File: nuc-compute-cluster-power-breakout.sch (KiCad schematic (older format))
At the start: 15 parts, among them J2 BM04B-SRSS-TB-LF-SN, J3 BM04B-SRSS-TB-LF-SN, J5 430450812, J6 430450812, J7 430450812, J8 430450812, J9 430450812, Q11 BC856,215

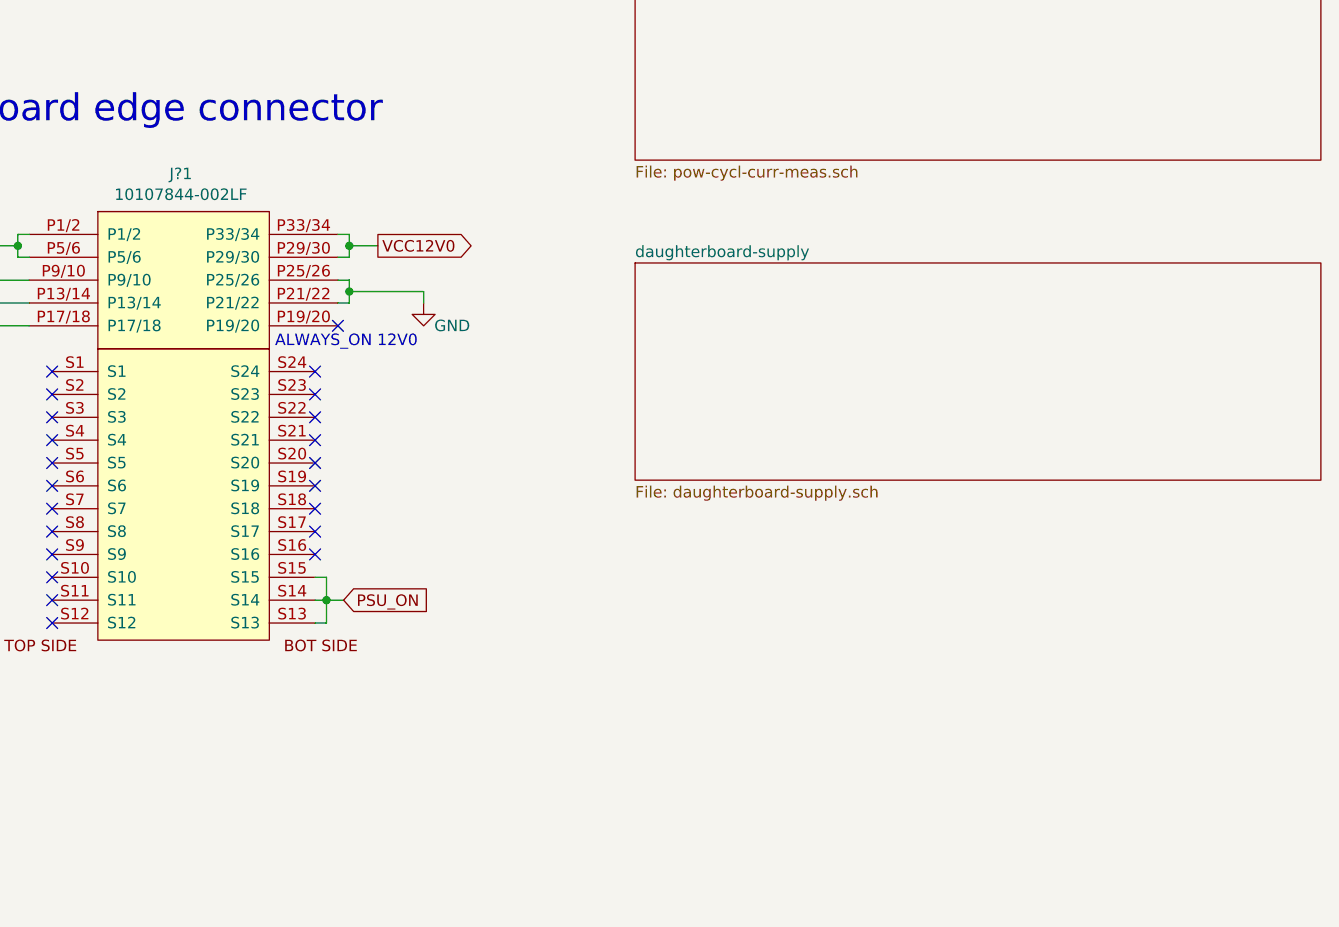
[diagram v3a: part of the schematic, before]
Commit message: Added stitching and mounting holes
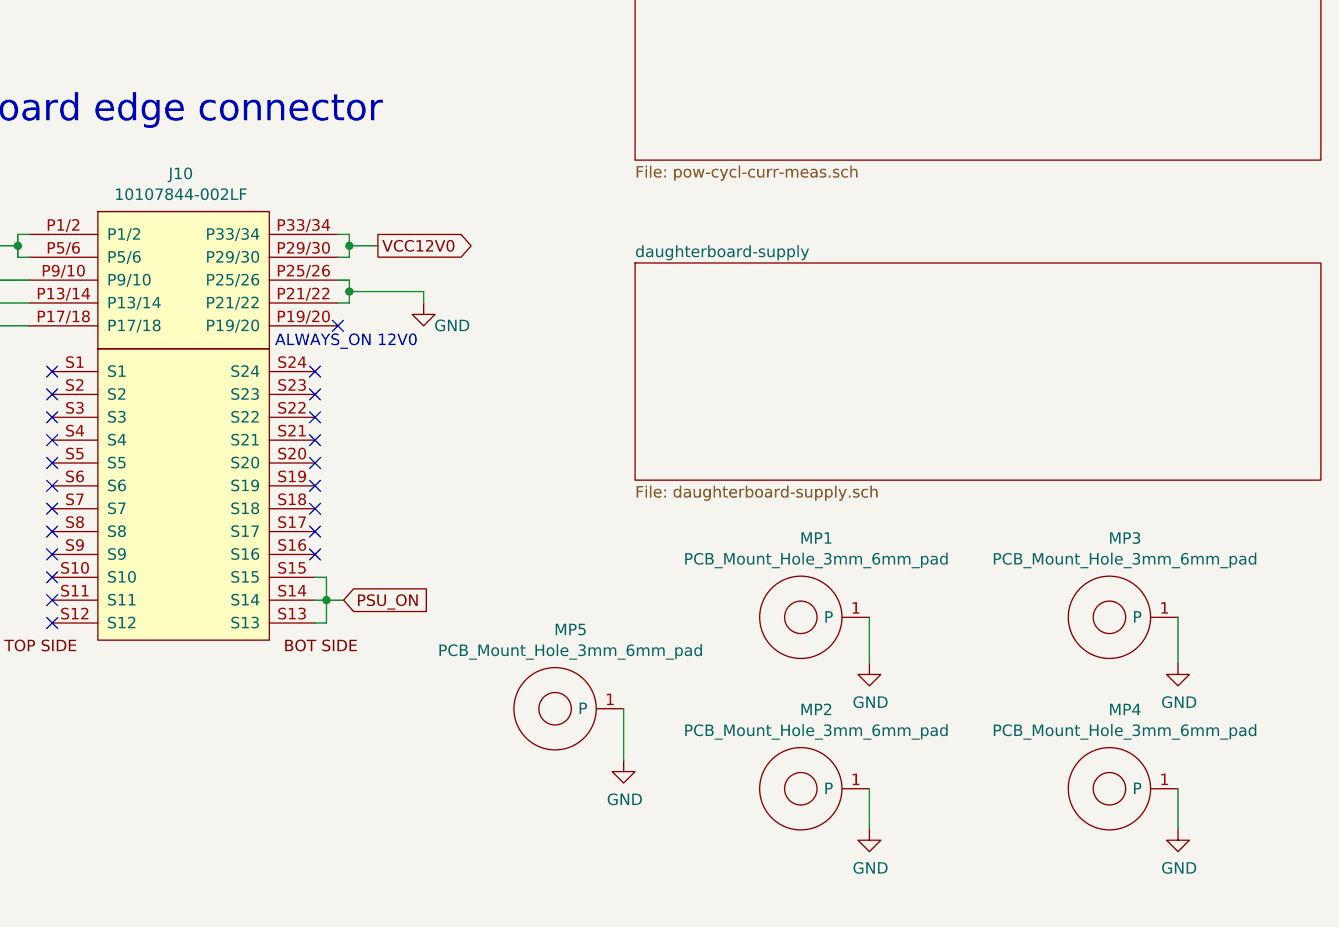
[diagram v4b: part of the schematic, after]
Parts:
- added MP1, MP2, MP3, MP4, MP5: PCB_Mount_Hole_3mm_6mm_pad, antmicro-footprints:mounting-hole-3.2mm, symbol antmicroMechanicalParts:PCB_Mount_Hole_3mm_6mm_pad
- renumbered J?1 to J10
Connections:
- net GND: now also MP1.1 (P), MP2.1 (P), MP3.1 (P), MP4.1 (P), MP5.1 (P)
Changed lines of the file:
@@
 ALWAYS_ON 12V0\n
 $Comp
-L antmicroRectangularConnectorsHeadersFemalePins:10107844-002LF J?1
+L antmicroRectangularConnectorsHeadersFemalePins:10107844-002LF J10
 U 1 1 624B9442
 P 5875 3475
-F 0 "J?1" H 5863 3515 50  0000 C CNN
+F 0 "J10" H 5863 3515 50  0000 C CNN
 F 1 "10107844-002LF" H 5863 3424 50  0000 C CNN
 F 2 "antmicro-footprints:10107844-002LF" H 5875 3550 50  0001 C CNN
@@
 Wire Wire Line
 	6200 975  6200 1200
+$Comp
+L antmicroMechanicalParts:PCB_Mount_Hole_3mm_6mm_pad MP1
+U 1 1 624D5C25
+P 8575 5375
+F 0 "MP1" H 8643 5720 50  0000 C CNN
+F 1 "PCB_Mount_Hole_3mm_6mm_pad" H 8643 5629 50  0000 C CNN
+F 2 "antmicro-footprints:mounting-hole-3.2mm" H 9375 6075 50  0001 C CNN
+F 3 "" H 9525 6175 50  0001 C CNN
+	1    8575 5375
+	1    0    0    -1
+$EndComp
+$Comp
+L antmicroMechanicalParts:PCB_Mount_Hole_3mm_6mm_pad MP3
+U 1 1 624DA217
+P 9925 5375
+F 0 "MP3" H 9993 5720 50  0000 C CNN
+F 1 "PCB_Mount_Hole_3mm_6mm_pad" H 9993 5629 50  0000 C CNN
+F 2 "antmicro-footprints:mounting-hole-3.2mm" H 10725 6075 50  0001 C CNN
+F 3 "" H 10875 6175 50  0001 C CNN
+	1    9925 5375
+	1    0    0    -1
+$EndComp
+$Comp
+L antmicroMechanicalParts:PCB_Mount_Hole_3mm_6mm_pad MP2
+U 1 1 624E49B1
+P 8575 6125
+F 0 "MP2" H 8643 6470 50  0000 C CNN
+F 1 "PCB_Mount_Hole_3mm_6mm_pad" H 8643 6379 50  0000 C CNN
+F 2 "antmicro-footprints:mounting-hole-3.2mm" H 9375 6825 50  0001 C CNN
+F 3 "" H 9525 6925 50  0001 C CNN
+	1    8575 6125
+	1    0    0    -1
+$EndComp
+$Comp
+L antmicroMechanicalParts:PCB_Mount_Hole_3mm_6mm_pad MP4
+U 1 1 624E49B7
+P 9925 6125
+F 0 "MP4" H 9993 6470 50  0000 C CNN
+F 1 "PCB_Mount_Hole_3mm_6mm_pad" H 9993 6379 50  0000 C CNN
+F 2 "antmicro-footprints:mounting-hole-3.2mm" H 10725 6825 50  0001 C CNN
+F 3 "" H 10875 6925 50  0001 C CNN
+	1    9925 6125
+	1    0    0    -1
+$EndComp
+$Comp
+L nuc-compute-cluster-power-breakout:GND #PWR073
+U 1 1 624E955A
+P 8875 6300
+F 0 "#PWR073" H 8875 6050 50  0001 C CNN
+F 1 "GND" H 8880 6127 50  0000 C CNN
+F 2 "" H 8875 6300 50  0001 C CNN
+F 3 "" H 8875 6300 50  0001 C CNN
+	1    8875 6300
+	1    0    0    -1
+$EndComp
+$Comp
+L nuc-compute-cluster-power-breakout:GND #PWR075
+U 1 1 624EA9FD
+P 10225 6300
+F 0 "#PWR075" H 10225 6050 50  0001 C CNN
+F 1 "GND" H 10230 6127 50  0000 C CNN
+F 2 "" H 10225 6300 50  0001 C CNN
+F 3 "" H 10225 6300 50  0001 C CNN
+	1    10225 6300
+	1    0    0    -1
+$EndComp
+$Comp
+L nuc-compute-cluster-power-breakout:GND #PWR072
+U 1 1 624EAD7E
+P 8875 5575
+F 0 "#PWR072" H 8875 5325 50  0001 C CNN
+F 1 "GND" H 8880 5402 50  0000 C CNN
+F 2 "" H 8875 5575 50  0001 C CNN
+F 3 "" H 8875 5575 50  0001 C CNN
+	1    8875 5575
+	1    0    0    -1
+$EndComp
+$Comp
+L nuc-compute-cluster-power-breakout:GND #PWR074
+U 1 1 624EB150
+P 10225 5575
+F 0 "#PWR074" H 10225 5325 50  0001 C CNN
+F 1 "GND" H 10230 5402 50  0000 C CNN
+F 2 "" H 10225 5575 50  0001 C CNN
+F 3 "" H 10225 5575 50  0001 C CNN
+	1    10225 5575
+	1    0    0    -1
+$EndComp
+Wire Wire Line
+	10225 5375 10225 5575
+Wire Wire Line
+	8875 5575 8875 5375
+Wire Wire Line
+	10225 6125 10225 6300
+Wire Wire Line
+	8875 6125 8875 6300
+$Comp
+L antmicroMechanicalParts:PCB_Mount_Hole_3mm_6mm_pad MP5
+U 1 1 62504F51
+P 7500 5775
+F 0 "MP5" H 7568 6120 50  0000 C CNN
+F 1 "PCB_Mount_Hole_3mm_6mm_pad" H 7568 6029 50  0000 C CNN
+F 2 "antmicro-footprints:mounting-hole-3.2mm" H 8300 6475 50  0001 C CNN
+F 3 "" H 8450 6575 50  0001 C CNN
+	1    7500 5775
+	1    0    0    -1
+$EndComp
+$Comp
+L nuc-compute-cluster-power-breakout:GND #PWR0106
+U 1 1 6250AA38
+P 7800 6000
+F 0 "#PWR0106" H 7800 5750 50  0001 C CNN
+F 1 "GND" H 7805 5827 50  0000 C CNN
+F 2 "" H 7800 6000 50  0001 C CNN
+F 3 "" H 7800 6000 50  0001 C CNN
+	1    7800 6000
+	1    0    0    -1
+$EndComp
+Wire Wire Line
+	7800 6000 7800 5775
 $EndSCHEMATC

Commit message: Loclib performed
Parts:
- D5: footprint antmicro-footprints:LED_0603 -> nuc-compute-cluster-power-breakout-footprints:LED_0603; symbol antmicroLEDIndicationDiscrete:LG_L29K-G2J1-24-Z -> nuc-compute-cluster-power-breakout:LG_L29K-G2J1-24-Z
- J10: footprint antmicro-footprints:10107844-002LF -> nuc-compute-cluster-power-breakout-footprints:10107844-002LF; symbol antmicroRectangularConnectorsHeadersFemalePins:10107844-002LF -> nuc-compute-cluster-power-breakout:10107844-002LF
- MP1, MP2, MP3, MP4, MP5: footprint antmicro-footprints:mounting-hole-3.2mm -> nuc-compute-cluster-power-breakout-footprints:mounting-hole-3.2mm; symbol antmicroMechanicalParts:PCB_Mount_Hole_3mm_6mm_pad -> nuc-compute-cluster-power-breakout:PCB_Mount_Hole_3mm_6mm_pad
- Q11: footprint antmicro-footprints:SOT-23-3 -> nuc-compute-cluster-power-breakout-footprints:SOT-23-3; symbol antmicroTransistorsBipolarSingle:BC856,215 -> nuc-compute-cluster-power-breakout:BC856,215
- R40: footprint antmicro-footprints:0402-res -> nuc-compute-cluster-power-breakout-footprints:0402-res; symbol antmicroResistors0402:R_10k_0402 -> nuc-compute-cluster-power-breakout:R_10k_0402
- R41: footprint antmicro-footprints:0402-res -> nuc-compute-cluster-power-breakout-footprints:0402-res; symbol antmicroResistors0402:R_680R_0402 -> nuc-compute-cluster-power-breakout:R_680R_0402
- S1: footprint antmicro-footprints:Switch_Slide_MSS3 -> nuc-compute-cluster-power-breakout-footprints:Switch_Slide_MSS3; symbol antmicroSlideSwitches:MSS3-V-T_R -> nuc-compute-cluster-power-breakout:MSS3-V-T_R
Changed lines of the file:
@@
 $EndComp
 $Comp
-L antmicroSlideSwitches:MSS3-V-T_R S1
+L nuc-compute-cluster-power-breakout:MSS3-V-T_R S1
 U 1 1 6270AED7
 P 5400 1750
 F 0 "S1" H 5150 1600 50  0000 C CNN
 F 1 "MSS3-V-T_R" H 5125 1500 50  0000 C CNN
-F 2 "antmicro-footprints:Switch_Slide_MSS3" H 5600 1950 50  0001 L CNN
+F 2 "nuc-compute-cluster-power-breakout-footprints:Switch_Slide_MSS3" H 5600 1950 50  0001 L CNN
 F 3 "https://pl.mouser.com/datasheet/2/910/605_MSS34-1571494.pdf" H 5600 2050 60  0001 L CNN
 F 4 "MSS3-V-T/R" H 5600 2250 60  0001 L CNN "MPN"
@@
 ALWAYS_ON 12V0\n
 $Comp
-L antmicroRectangularConnectorsHeadersFemalePins:10107844-002LF J10
+L nuc-compute-cluster-power-breakout:10107844-002LF J10
 U 1 1 624B9442
 P 5875 3475
 F 0 "J10" H 5863 3515 50  0000 C CNN
 F 1 "10107844-002LF" H 5863 3424 50  0000 C CNN
-F 2 "antmicro-footprints:10107844-002LF" H 5875 3550 50  0001 C CNN
+F 2 "nuc-compute-cluster-power-breakout-footprints:10107844-002LF" H 5875 3550 50  0001 C CNN
 F 3 "https://www.farnell.com/cad/2569863.pdf" H 5875 3550 50  0001 C CNN
 F 4 "10107844-002LF" H 5900 3550 50  0001 C CNN "MPN"
@@
 NoConn ~ 5300 5200
 $Comp
-L antmicroLEDIndicationDiscrete:LG_L29K-G2J1-24-Z D5
+L nuc-compute-cluster-power-breakout:LG_L29K-G2J1-24-Z D5
 U 1 1 62565FEC
 P 6200 1850
 F 0 "D5" V 6097 2028 60  0000 L CNN
 F 1 "LG_L29K-G2J1-24-Z" V 6203 2028 60  0000 L CNN
-F 2 "antmicro-footprints:LED_0603" H 6400 2050 60  0001 L CNN
+F 2 "nuc-compute-cluster-power-breakout-footprints:LED_0603" H 6400 2050 60  0001 L CNN
 F 3 "https://dammedia.osram.info/media/resource/hires/osram-dam-2493945/LG%20L29K.pdf" H 6400 2150 60  0001 L CNN
 F 4 "LG L29K-G2J1-24-Z" H 6400 2350 60  0001 L CNN "MPN"
@@
 	6200 1650 6200 1600
 $Comp
-L antmicroResistors0402:R_10k_0402 R40
+L nuc-compute-cluster-power-breakout:R_10k_0402 R40
 U 1 1 625AFF56
 P 5550 1400
 F 0 "R40" H 5550 1187 60  0000 C CNN
 F 1 "R_10k_0402" H 5550 1250 60  0001 C CNN
-F 2 "antmicro-footprints:0402-res" H 5750 1600 60  0001 L CNN
+F 2 "nuc-compute-cluster-power-breakout-footprints:0402-res" H 5750 1600 60  0001 L CNN
 F 3 "" H 5550 1400 50  0001 C CNN
 F 4 "VISHAY" H 5750 1800 60  0001 L CNN "Manufacturer"
@@
 	5700 1400 5900 1400
 $Comp
-L antmicroResistors0402:R_680R_0402 R41
+L nuc-compute-cluster-power-breakout:R_680R_0402 R41
 U 1 1 625B75CB
 P 6200 2150
 F 0 "R41" V 6155 2220 60  0000 L CNN
 F 1 "R_680R_0402" H 6200 2000 60  0001 C CNN
-F 2 "antmicro-footprints:0402-res" H 6400 2350 60  0001 L CNN
+F 2 "nuc-compute-cluster-power-breakout-footprints:0402-res" H 6400 2350 60  0001 L CNN
 F 3 "" H 6200 2150 50  0001 C CNN
 F 4 "ROYAL_OHM" H 6400 2550 60  0001 L CNN "Manufacturer"
@@
 	5675 1850 5675 2350
 $Comp
-L antmicroTransistorsBipolarSingle:BC856,215 Q11
+L nuc-compute-cluster-power-breakout:BC856,215 Q11
 U 1 1 625D60DF
 P 6100 1400
 F 0 "Q11" H 6290 1446 50  0000 L CNN
 F 1 "BC856,215" H 6290 1355 50  0000 L CNN
-F 2 "antmicro-footprints:SOT-23-3" H 6900 1100 50  0001 C CNN
+F 2 "nuc-compute-cluster-power-breakout-footprints:SOT-23-3" H 6900 1100 50  0001 C CNN
 F 3 "https://www.farnell.com/datasheets/490737.pdf" H 6100 1350 50  0001 C CNN
 F 4 "BC856,215" H 6550 1200 50  0001 C CNN "MPN"
@@
 	6200 975  6200 1200
 $Comp
-L antmicroMechanicalParts:PCB_Mount_Hole_3mm_6mm_pad MP1
+L nuc-compute-cluster-power-breakout:PCB_Mount_Hole_3mm_6mm_pad MP1
 U 1 1 624D5C25
 P 8575 5375
 F 0 "MP1" H 8643 5720 50  0000 C CNN
 F 1 "PCB_Mount_Hole_3mm_6mm_pad" H 8643 5629 50  0000 C CNN
-F 2 "antmicro-footprints:mounting-hole-3.2mm" H 9375 6075 50  0001 C CNN
+F 2 "nuc-compute-cluster-power-breakout-footprints:mounting-hole-3.2mm" H 9375 6075 50  0001 C CNN
 F 3 "" H 9525 6175 50  0001 C CNN
 	1    8575 5375
@@
 $EndComp
 $Comp
-L antmicroMechanicalParts:PCB_Mount_Hole_3mm_6mm_pad MP3
+L nuc-compute-cluster-power-breakout:PCB_Mount_Hole_3mm_6mm_pad MP3
 U 1 1 624DA217
 P 9925 5375
 F 0 "MP3" H 9993 5720 50  0000 C CNN
 F 1 "PCB_Mount_Hole_3mm_6mm_pad" H 9993 5629 50  0000 C CNN
-F 2 "antmicro-footprints:mounting-hole-3.2mm" H 10725 6075 50  0001 C CNN
+F 2 "nuc-compute-cluster-power-breakout-footprints:mounting-hole-3.2mm" H 10725 6075 50  0001 C CNN
 F 3 "" H 10875 6175 50  0001 C CNN
 	1    9925 5375
@@
 $EndComp
 $Comp
-L antmicroMechanicalParts:PCB_Mount_Hole_3mm_6mm_pad MP2
+L nuc-compute-cluster-power-breakout:PCB_Mount_Hole_3mm_6mm_pad MP2
 U 1 1 624E49B1
 P 8575 6125
 F 0 "MP2" H 8643 6470 50  0000 C CNN
 F 1 "PCB_Mount_Hole_3mm_6mm_pad" H 8643 6379 50  0000 C CNN
-F 2 "antmicro-footprints:mounting-hole-3.2mm" H 9375 6825 50  0001 C CNN
+F 2 "nuc-compute-cluster-power-breakout-footprints:mounting-hole-3.2mm" H 9375 6825 50  0001 C CNN
 F 3 "" H 9525 6925 50  0001 C CNN
 	1    8575 6125
@@
 $EndComp
 $Comp
-L antmicroMechanicalParts:PCB_Mount_Hole_3mm_6mm_pad MP4
+L nuc-compute-cluster-power-breakout:PCB_Mount_Hole_3mm_6mm_pad MP4
 U 1 1 624E49B7
 P 9925 6125
 F 0 "MP4" H 9993 6470 50  0000 C CNN
 F 1 "PCB_Mount_Hole_3mm_6mm_pad" H 9993 6379 50  0000 C CNN
-F 2 "antmicro-footprints:mounting-hole-3.2mm" H 10725 6825 50  0001 C CNN
+F 2 "nuc-compute-cluster-power-breakout-footprints:mounting-hole-3.2mm" H 10725 6825 50  0001 C CNN
 F 3 "" H 10875 6925 50  0001 C CNN
 	1    9925 6125
@@
 	8875 6125 8875 6300
 $Comp
-L antmicroMechanicalParts:PCB_Mount_Hole_3mm_6mm_pad MP5
+L nuc-compute-cluster-power-breakout:PCB_Mount_Hole_3mm_6mm_pad MP5
 U 1 1 62504F51
 P 7500 5775
 F 0 "MP5" H 7568 6120 50  0000 C CNN
 F 1 "PCB_Mount_Hole_3mm_6mm_pad" H 7568 6029 50  0000 C CNN
-F 2 "antmicro-footprints:mounting-hole-3.2mm" H 8300 6475 50  0001 C CNN
+F 2 "nuc-compute-cluster-power-breakout-footprints:mounting-hole-3.2mm" H 8300 6475 50  0001 C CNN
 F 3 "" H 8450 6575 50  0001 C CNN
 	1    7500 5775
